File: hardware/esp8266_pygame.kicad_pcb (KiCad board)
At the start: 2 copper layers, 104.7 x 66.1 mm, 80 parts, among them J1 Conn_02x02_Odd_Even, J2 Conn_01x02, J3 USB_C_Receptacle_USB2.0_16P, J4 Conn_01x08, J5 Conn_01x08, J6 Conn_01x08, Q1 PNP, SW1 SW_Push, SW2 SW_Push, SW3 SW_Push, SW4 SW_Push, SW5 SW_Push, SW6 SW_Push, SW7 SW_Push, SW8 SW_Push, U1 ESP-07, U2 SW_SPDT_3pin, U3 HX3242, U4 TP4056, U5 FS8502A, U6 DW01A, U7 AP2112K-3.3, U8 PCF8574T, U9 LM386

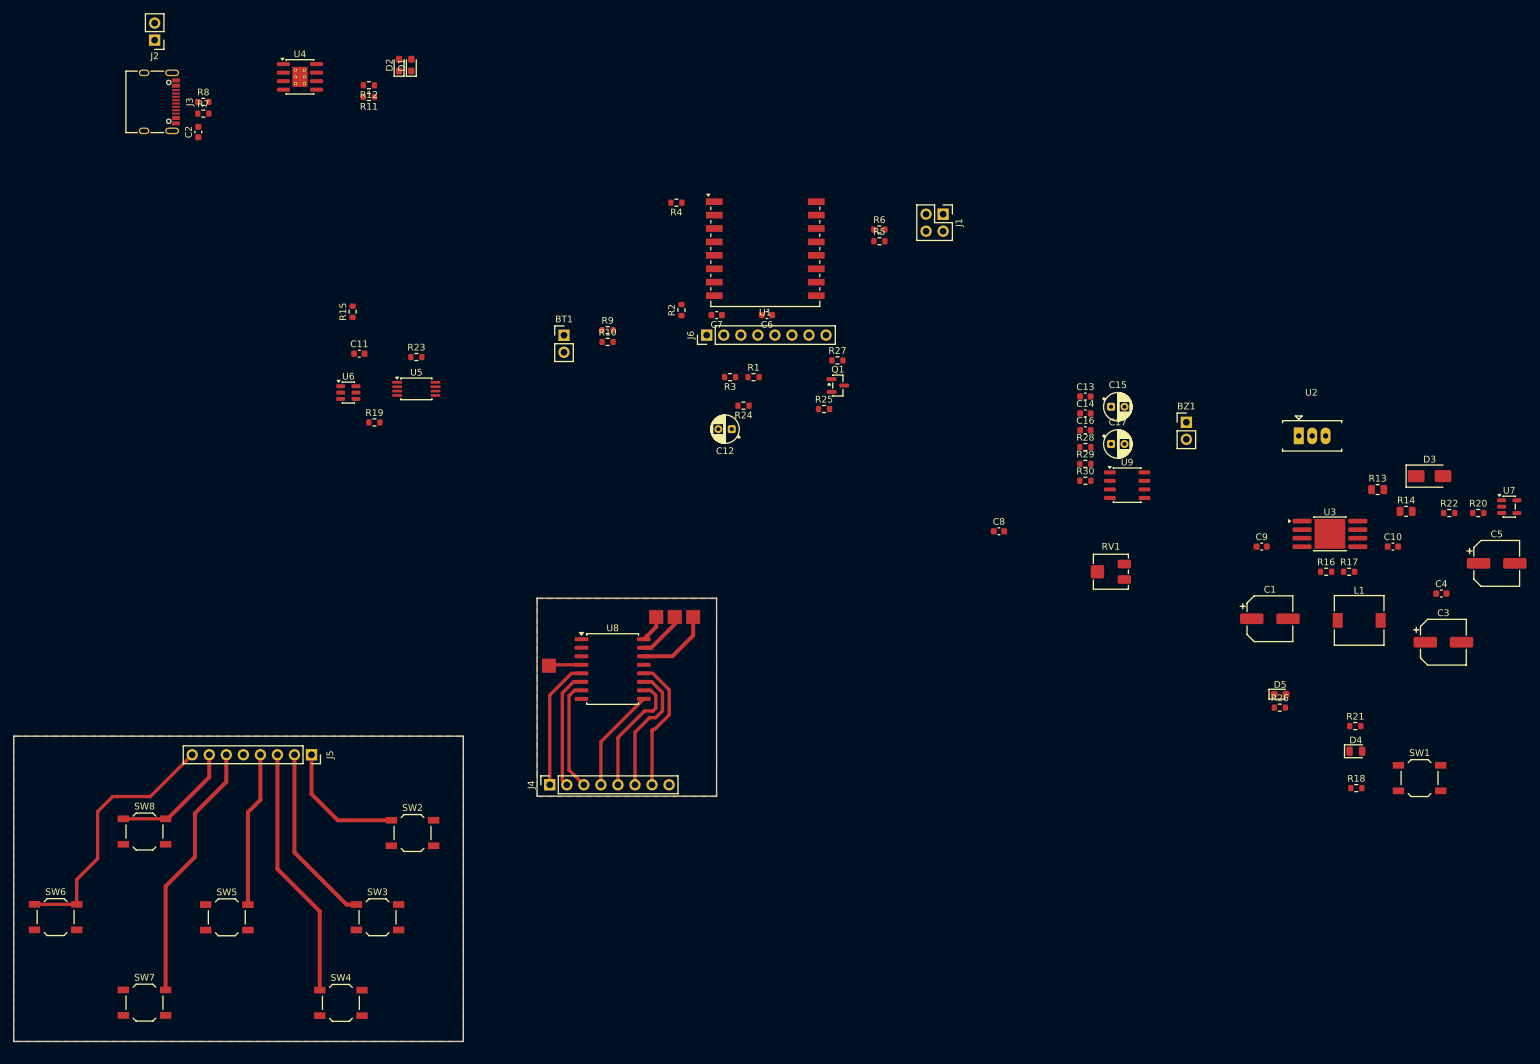
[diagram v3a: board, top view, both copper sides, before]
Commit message: Add PCB edges marks
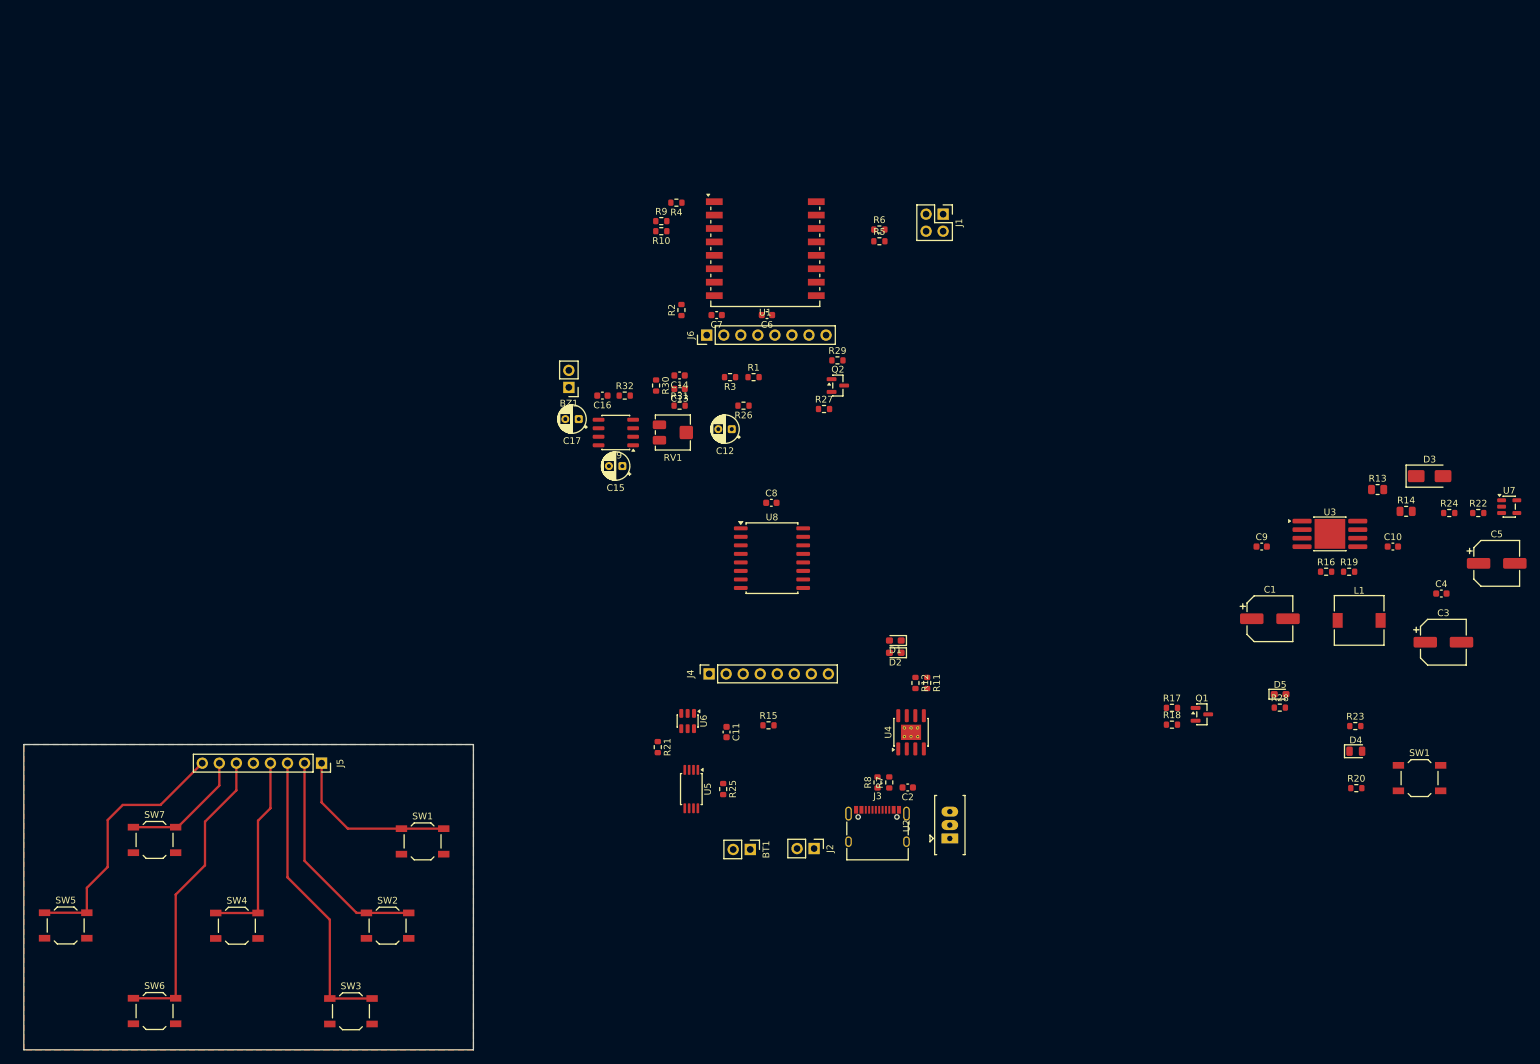
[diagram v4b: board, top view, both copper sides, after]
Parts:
- added Q1: PNP, Package_TO_SOT_SMD:SOT-23, F.Cu at (189.6, 142.0)
- added R17: 10k, Resistor_SMD:R_0603_1608Metric, F.Cu at (185.1, 141.0)
- added R18: 1k, Resistor_SMD:R_0603_1608Metric, F.Cu at (185.1, 143.5)
- moved J2 155.5 mm to (131.8, 162.0), turned to -90 degrees
- moved J3 153.7 mm to (141.2, 159.9), turned to 0 degrees
- moved C2 143.9 mm to (145.7, 152.9), turned to 180 degrees
- moved R7 142.8 mm to (143.0, 152.2), turned to 90 degrees
- moved R8 142.8 mm to (141.2, 152.2), turned to 90 degrees
- moved U4 133.5 mm to (146.2, 144.7), turned to 90 degrees
- moved R12 120.7 mm to (146.9, 137.3), turned to -90 degrees
- moved R11 120.6 mm to (148.6, 137.3), turned to -90 degrees
- moved D2 114.6 mm to (143.9, 132.8), turned to 180 degrees
- moved D1 112.0 mm to (143.9, 131.0), turned to 180 degrees
- moved BZ1 92.2 mm to (95.2, 93.3), turned to 180 degrees
- moved U2 87.7 mm to (146.0, 158.6), turned to 90 degrees
- moved R15 87.4 mm to (125.0, 143.6), turned to 0 degrees
- moved BT1 81.5 mm to (122.2, 162.1), turned to -90 degrees
- moved C17 79.4 mm to (96.7, 98.0), turned to 180 degrees
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- renumbered Q1 to Q2, R17 to R19, R18 to R20, R19 to R21, R20 to R22, R21 to R23, R22 to R24, R23 to R25, R24 to R26, R25 to R27, R26 to R28, R27 to R29, R28 to R30, R29 to R31, R30 to R32, SW2 to SW1, SW3 to SW2, SW4 to SW3, SW5 to SW4, SW6 to SW5, SW7 to SW6, SW8 to SW7
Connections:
- D4 pad 1: Net-(D4-K) -> /Human Machine Interface Section/C_Button_CONN
- D4 pad 2: /Human Machine Interface Section/POWER_EN -> Net-(D4-A)
- R10 pad 1: +BATT -> /Ubatt
- R19 pad 1: Net-(D4-K) -> Net-(R19-Pad1)
- R20 pad 1: Net-(D4-K) -> Net-(R19-Pad1)
- R20 pad 2: Net-(R18-Pad2) -> Net-(Q1-C)
- R22 pad 2: Net-(D4-K) -> Net-(R19-Pad1)
- R23 pad 1: Net-(D4-K) -> Net-(R19-Pad1)
- R9 pad 2: +BATT -> /Ubatt
- U1 pad 2: +BATT -> /Ubatt
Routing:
- net /Human Machine Interface Section/UP_Button_CONN: track 20.2 -> 0.00 mm
- net /Human Machine Interface Section/A_Button_CONN: track 19.4 -> 0.00 mm
- net /Human Machine Interface Section/Down_Button_CONN: track 19.4 -> 0.00 mm
- net /Human Machine Interface Section/Left_Button_CONN: track 18.5 -> 0.00 mm
- net /Human Machine Interface Section/B_Button_CONN: track 17.5 -> 0.00 mm
- net /Human Machine Interface Section/C_Button_CONN: track 16.4 -> 0.00 mm
- net /Human Machine Interface Section/Right_Button_CONN: track 15.5 -> 0.00 mm
- net /SCL: track 11.6 -> 0.00 mm
- net /SDA: track 7.38 -> 0.00 mm
- net /Human Machine Interface Section/A_Button: track 19.4 -> 25.7 mm
- net /Human Machine Interface Section/Down_Button: track 38.8 -> 45.1 mm
- net /Human Machine Interface Section/C_Button: track 37.7 -> 44.0 mm
- net /Human Machine Interface Section/B_Button: track 27.0 -> 33.3 mm
- net /Human Machine Interface Section/Right_Button: track 23.1 -> 29.4 mm
- net /Human Machine Interface Section/POWER_EN: track 4.91 -> 0.00 mm
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- removed copper zone on F.Cu, net GND
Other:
- board size 104.7 x 66.1 mm -> 67 x 45.5 mm
